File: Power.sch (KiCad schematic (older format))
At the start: 18 parts, among them P1 24-pin Mini-Fit Jr., SW1 Power Switch

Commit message: Back-annotated footprints into the schematic
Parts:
- C13, C3, C4: footprint (none) -> Capacitors_SMD:c_1206
- JP1, JP2, JP3, JP4: footprint (none) -> BenchBudEE:GND_POINT
- L2, L3, L4: footprint (none) -> SMD_Packages:SM1210L
- P1: footprint (none) -> BenchBudEE:ATX_Header
- R8: footprint (none) -> SMD_Packages:SM0805
- STAR1: footprint (none) -> Connect:1pin
- SW1: footprint (none) -> BenchBudEE:BB_switch
- TH1, TH2, TH3, TH4: footprint (none) -> SMD_Packages:SM1812
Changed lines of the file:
@@
 F 0 "P1" H 2100 3000 60  0000 C CNN
 F 1 "24-pin Mini-Fit Jr." V 2100 2350 50  0000 C CNN
-F 2 "" H 2100 2350 60  0000 C CNN
+F 2 "BenchBudEE:ATX_Header" H 2100 2350 60  0001 C CNN
 F 3 "" H 2100 2350 60  0000 C CNN
 F 4 "Molex" H 2100 2350 60  0001 C CNN "MFG Name"
@@
 F 0 "SW1" H 3300 3350 50  0000 C CNN
 F 1 "Power Switch" H 3350 3050 50  0000 C CNN
-F 2 "" H 3500 3200 60  0000 C CNN
+F 2 "BenchBudEE:BB_switch" H 3500 3200 60  0001 C CNN
 F 3 "" H 3500 3200 60  0000 C CNN
 F 4 "C&K Components" H 3500 3200 60  0001 C CNN "MFG Name"
@@
 F 0 "R8" V 4730 3100 40  0000 C CNN
 F 1 "0" V 4657 3101 40  0000 C CNN
-F 2 "" V 4580 3100 30  0000 C CNN
+F 2 "SMD_Packages:SM0805" V 4580 3100 30  0001 C CNN
 F 3 "" H 4650 3100 30  0000 C CNN
 	1    4650 3100
@@
 F 0 "L3" V 7100 2350 40  0000 C CNN
 F 1 "CM322522-220KL" V 7250 2350 40  0000 C CNN
-F 2 "" H 7150 2350 60  0000 C CNN
+F 2 "SMD_Packages:SM1210L" H 7150 2350 60  0001 C CNN
 F 3 "" H 7150 2350 60  0000 C CNN
 F 4 "Bourns" H 7150 2350 60  0001 C CNN "MFG Name"
@@
 F 0 "C4" H 7800 3350 40  0000 L CNN
 F 1 "10u" H 7806 3165 40  0000 L CNN
-F 2 "" H 7838 3100 30  0000 C CNN
+F 2 "Capacitors_SMD:c_1206" H 7838 3100 30  0001 C CNN
 F 3 "" H 7800 3250 60  0000 C CNN
 	1    7800 3250
@@
 F 0 "C3" H 7800 2750 40  0000 L CNN
 F 1 "10u" H 7806 2565 40  0000 L CNN
-F 2 "" H 7838 2500 30  0000 C CNN
+F 2 "Capacitors_SMD:c_1206" H 7838 2500 30  0001 C CNN
 F 3 "" H 7800 2650 60  0000 C CNN
 	1    7800 2650
@@
 F 0 "TH1" V 3350 1850 50  0000 C CNN
 F 1 "MINISMDC050F-2" V 3150 1800 50  0000 C CNN
-F 2 "" H 3250 1800 60  0000 C CNN
+F 2 "SMD_Packages:SM1812" H 3250 1800 60  0001 C CNN
 F 3 "" H 3250 1800 60  0000 C CNN
 F 4 "TE Connectivity" H 3250 1800 60  0001 C CNN "MFG Name"
@@
 F 0 "TH2" V 3850 2050 50  0000 C CNN
 F 1 "MINISMDC050F-2" V 3650 2000 50  0000 C CNN
-F 2 "" H 3750 2000 60  0000 C CNN
+F 2 "SMD_Packages:SM1812" H 3750 2000 60  0001 C CNN
 F 3 "" H 3750 2000 60  0000 C CNN
 F 4 "TE Connectivity" H 3750 2000 60  0001 C CNN "MFG Name"
@@
 F 0 "TH3" V 4350 2250 50  0000 C CNN
 F 1 "MINISMDC050F-2" V 4150 2200 50  0000 C CNN
-F 2 "" H 4250 2200 60  0000 C CNN
+F 2 "SMD_Packages:SM1812" H 4250 2200 60  0001 C CNN
 F 3 "" H 4250 2200 60  0000 C CNN
 F 4 "TE Connectivity" H 4250 2200 60  0001 C CNN "MFG Name"
@@
 F 0 "TH4" V 4850 2450 50  0000 C CNN
 F 1 "MINISMDC050F-2" V 4650 2400 50  0000 C CNN
-F 2 "" H 4750 2400 60  0000 C CNN
+F 2 "SMD_Packages:SM1812" H 4750 2400 60  0001 C CNN
 F 3 "" H 4750 2400 60  0000 C CNN
 F 4 "TE Connectivity" H 4750 2400 60  0001 C CNN "MFG Name"
@@
 F 0 "L4" V 7100 1050 40  0000 C CNN
 F 1 "CM322522-220KL" V 7250 1050 40  0000 C CNN
-F 2 "" H 7150 1050 60  0000 C CNN
+F 2 "SMD_Packages:SM1210L" H 7150 1050 60  0001 C CNN
 F 3 "" H 7150 1050 60  0000 C CNN
 F 4 "Bourns" H 7150 1050 60  0001 C CNN "MFG Name"
@@
 F 0 "C13" H 7800 1450 40  0000 L CNN
 F 1 "10u" H 7806 1265 40  0000 L CNN
-F 2 "" H 7838 1200 30  0000 C CNN
+F 2 "Capacitors_SMD:c_1206" H 7838 1200 30  0001 C CNN
 F 3 "" H 7800 1350 60  0000 C CNN
 	1    7800 1350
@@
 F 0 "L2" V 7050 3550 40  0000 C CNN
 F 1 "CM322522-220KL" V 7200 3550 40  0000 C CNN
-F 2 "" H 7100 3550 60  0000 C CNN
+F 2 "SMD_Packages:SM1210L" H 7100 3550 60  0001 C CNN
 F 3 "" H 7100 3550 60  0000 C CNN
 F 4 "Bourns" H 7100 3550 60  0001 C CNN "MFG Name"
@@
 F 0 "STAR1" H 3080 5150 40  0000 L CNN
 F 1 "CONN_1" H 3000 5205 30  0001 C CNN
-F 2 "" H 3000 5150 60  0000 C CNN
+F 2 "Connect:1pin" H 3000 5150 60  0001 C CNN
 F 3 "" H 3000 5150 60  0000 C CNN
 	1    3000 5150
@@
 F 0 "JP1" H 3700 5850 60  0000 C CNN
 F 1 "JUMPER" H 3700 5620 40  0000 C CNN
-F 2 "" H 3700 5700 60  0000 C CNN
+F 2 "BenchBudEE:GND_POINT" H 3700 5700 60  0001 C CNN
 F 3 "" H 3700 5700 60  0000 C CNN
 	1    3700 5700
@@
 F 0 "JP2" H 3700 6250 60  0000 C CNN
 F 1 "JUMPER" H 3700 6020 40  0000 C CNN
-F 2 "" H 3700 6100 60  0000 C CNN
+F 2 "BenchBudEE:GND_POINT" H 3700 6100 60  0001 C CNN
 F 3 "" H 3700 6100 60  0000 C CNN
 	1    3700 6100
@@
 F 0 "JP3" H 3700 6650 60  0000 C CNN
 F 1 "JUMPER" H 3700 6420 40  0000 C CNN
-F 2 "" H 3700 6500 60  0000 C CNN
+F 2 "BenchBudEE:GND_POINT" H 3700 6500 60  0001 C CNN
 F 3 "" H 3700 6500 60  0000 C CNN
 	1    3700 6500
@@
 F 0 "JP4" H 3700 7050 60  0000 C CNN
 F 1 "JUMPER" H 3700 6820 40  0000 C CNN
-F 2 "" H 3700 6900 60  0000 C CNN
+F 2 "BenchBudEE:GND_POINT" H 3700 6900 60  0001 C CNN
 F 3 "" H 3700 6900 60  0000 C CNN
 	1    3700 6900

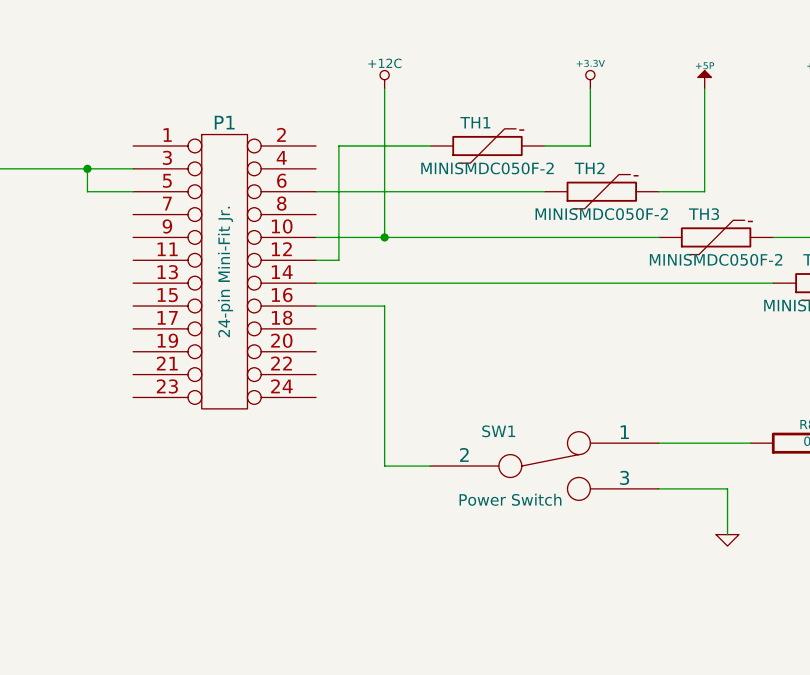
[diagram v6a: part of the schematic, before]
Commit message: Final part numbers added to schematic, cross-checked KiCAD BOM against manual BOM
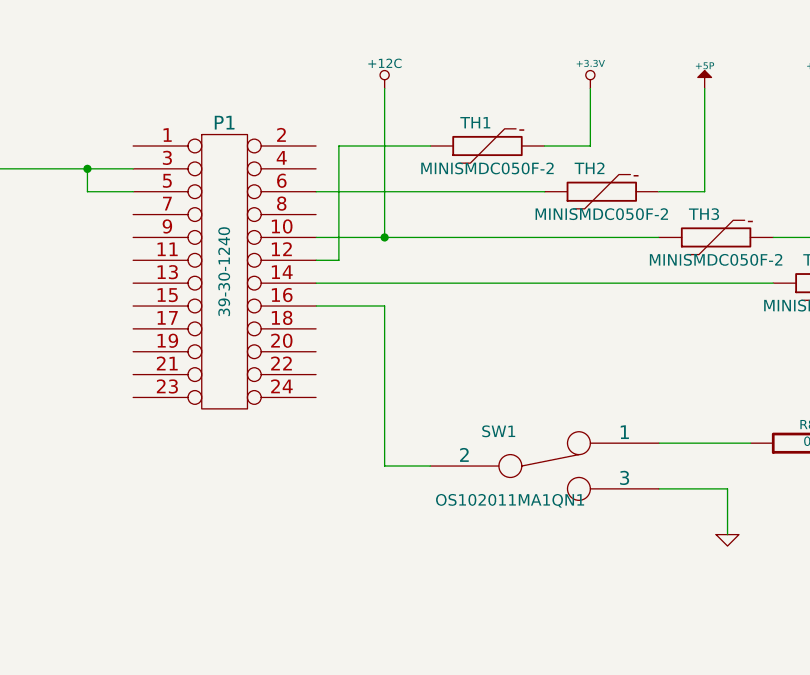
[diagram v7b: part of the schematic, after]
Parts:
- P1: value 24-pin Mini-Fit Jr. -> 39-30-1240
- SW1: value Power Switch -> OS102011MA1QN1
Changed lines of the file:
@@
 P 2100 2350
 F 0 "P1" H 2100 3000 60  0000 C CNN
-F 1 "24-pin Mini-Fit Jr." V 2100 2350 50  0000 C CNN
+F 1 "39-30-1240" V 2100 2350 50  0000 C CNN
 F 2 "BenchBudEE:ATX_Header" H 2100 2350 60  0001 C CNN
 F 3 "" H 2100 2350 60  0000 C CNN
@@
 P 3500 3200
 F 0 "SW1" H 3300 3350 50  0000 C CNN
-F 1 "Power Switch" H 3350 3050 50  0000 C CNN
+F 1 "OS102011MA1QN1" H 3350 3050 50  0000 C CNN
 F 2 "BenchBudEE:BB_switch" H 3500 3200 60  0001 C CNN
 F 3 "" H 3500 3200 60  0000 C CNN
